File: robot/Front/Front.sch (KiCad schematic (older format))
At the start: 43 parts, among them J1 USB_B_Micro, Q1 BC849, Q2 BC849, SW2 SW_Push, U1 CH340C, U10 ESP32-WROOM-32, U2 CJVL53L0XV2, U3 LD1117S33CTR

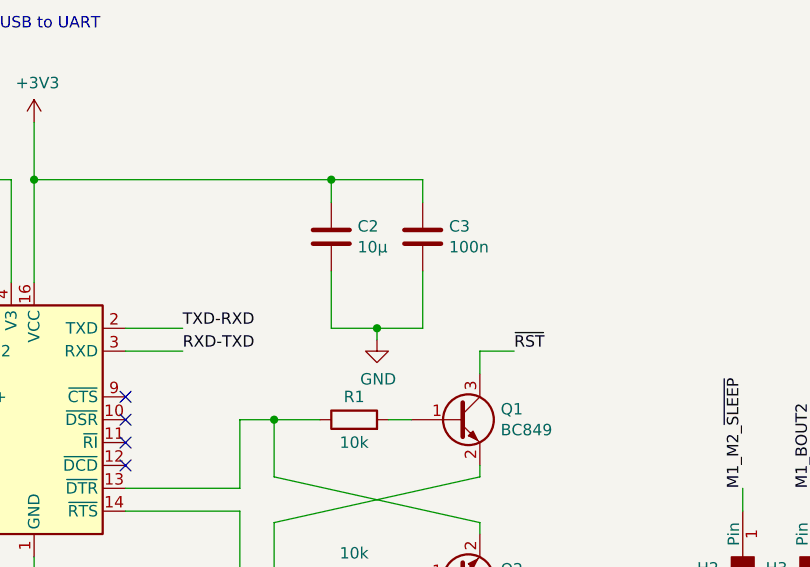
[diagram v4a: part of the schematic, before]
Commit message: Shrink design
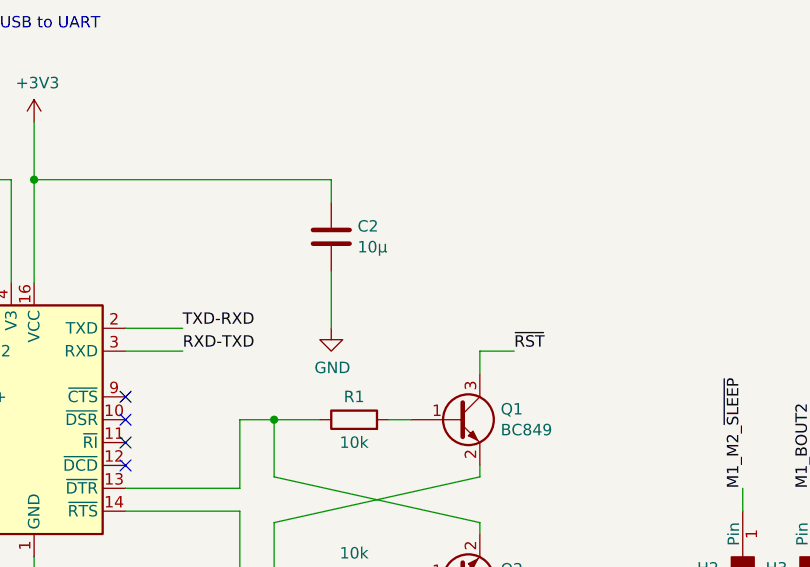
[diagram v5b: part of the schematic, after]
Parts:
- removed C3: 100n, Capacitors_SMD:C_1206, symbol Device:C
- C1, C2, C6: footprint Capacitors_SMD:C_1206 -> Capacitors_SMD:C_0805
- R1, R18, R2, R3, R4: footprint Resistors_SMD:R_1206 -> Resistors_SMD:R_0805
- U2: footprint Custom:CJVL53L0XV2_NoMountHoles -> Custom:GYVL53L0X_NoMountingHoles
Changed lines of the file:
@@
 F 0 "R18" H 8070 1196 50  0000 L CNN
 F 1 "10k" H 8070 1105 50  0000 L CNN
-F 2 "Resistors_SMD:R_1206" V 7930 1150 50  0001 C CNN
+F 2 "Resistors_SMD:R_0805" V 7930 1150 50  0001 C CNN
 F 3 "~" H 8000 1150 50  0001 C CNN
 	1    8000 1150
@@
 F 0 "C1" H 2365 1846 50  0000 L CNN
 F 1 "100n" H 2365 1755 50  0000 L CNN
-F 2 "Capacitors_SMD:C_1206" H 2288 1650 50  0001 C CNN
+F 2 "Capacitors_SMD:C_0805" H 2288 1650 50  0001 C CNN
 F 3 "~" H 2250 1800 50  0001 C CNN
 	1    2250 1800
@@
 $Comp
 L Device:C C?
-U 1 1 5D727709
-P 4450 1850
-AR Path="/5D17B31F/5D727709" Ref="C?"  Part="1"
-AR Path="/5D179377/5D727709" Ref="C?"  Part="1"
-AR Path="/5D727709" Ref="C3"  Part="1"
-F 0 "C3" H 4565 1896 50  0000 L CNN
-F 1 "100n" H 4565 1805 50  0000 L CNN
-F 2 "Capacitors_SMD:C_1206" H 4488 1700 50  0001 C CNN
-F 3 "~" H 4450 1850 50  0001 C CNN
-	1    4450 1850
-	1    0    0    -1
-$EndComp
-$Comp
-L Device:C C?
 U 1 1 5D72A7A5
 P 4050 1850
@@
 F 0 "C2" H 4165 1896 50  0000 L CNN
 F 1 "10µ" H 4165 1805 50  0000 L CNN
-F 2 "Capacitors_SMD:C_1206" H 4088 1700 50  0001 C CNN
+F 2 "Capacitors_SMD:C_0805" H 4088 1700 50  0001 C CNN
 F 3 "~" H 4050 1850 50  0001 C CNN
 	1    4050 1850
@@
 	4050 1700 4050 1600
 Wire Wire Line
-	4450 1700 4450 1600
-Wire Wire Line
-	4050 1600 4450 1600
-Wire Wire Line
 	2250 1950 2250 2050
 Wire Wire Line
@@
 L power:GND #PWR?
 U 1 1 5D72771A
-P 4250 2300
+P 4050 2250
 AR Path="/5D17B31F/5D72771A" Ref="#PWR?"  Part="1"
 AR Path="/5D179377/5D72771A" Ref="#PWR?"  Part="1"
 AR Path="/5D72771A" Ref="#PWR03"  Part="1"
-F 0 "#PWR03" H 4250 2050 50  0001 C CNN
-F 1 "GND" H 4255 2127 50  0000 C CNN
-F 2 "" H 4250 2300 50  0001 C CNN
-F 3 "" H 4250 2300 50  0001 C CNN
-	1    4250 2300
-	1    0    0    -1
-$EndComp
-Wire Wire Line
-	4250 2250 4450 2250
-Wire Wire Line
-	4450 2250 4450 2000
-Wire Wire Line
-	4250 2250 4250 2300
-Wire Wire Line
-	4050 2250 4250 2250
+F 0 "#PWR03" H 4050 2000 50  0001 C CNN
+F 1 "GND" H 4055 2077 50  0000 C CNN
+F 2 "" H 4050 2250 50  0001 C CNN
+F 3 "" H 4050 2250 50  0001 C CNN
+	1    4050 2250
+	1    0    0    -1
+$EndComp
 Wire Wire Line
 	4050 2000 4050 2250
-Connection ~ 4250 2250
 Wire Wire Line
 	2750 1600 4050 1600
@@
 Wire Wire Line
 	2750 1600 2750 2050
-Connection ~ 4050 1600
 NoConn ~ 3150 2550
 NoConn ~ 3150 2650
@@
 F 0 "R1" V 4250 2650 50  0000 C CNN
 F 1 "10k" V 4050 2650 50  0000 C CNN
-F 2 "Resistors_SMD:R_1206" V 4080 2650 50  0001 C CNN
+F 2 "Resistors_SMD:R_0805" V 4080 2650 50  0001 C CNN
 F 3 "~" H 4150 2650 50  0001 C CNN
 	1    4150 2650
@@
 F 0 "R2" V 4250 3350 50  0000 C CNN
 F 1 "10k" V 4034 3350 50  0000 C CNN
-F 2 "Resistors_SMD:R_1206" V 4080 3350 50  0001 C CNN
+F 2 "Resistors_SMD:R_0805" V 4080 3350 50  0001 C CNN
 F 3 "~" H 4150 3350 50  0001 C CNN
 	1    4150 3350
@@
 F 0 "R3" H 9630 5254 50  0000 R CNN
 F 1 "150" H 9630 5345 50  0000 R CNN
-F 2 "Resistors_SMD:R_1206" V 9630 5300 50  0001 C CNN
+F 2 "Resistors_SMD:R_0805" V 9630 5300 50  0001 C CNN
 F 3 "~" H 9700 5300 50  0001 C CNN
 	1    9700 5300
@@
 F 0 "R4" H 10630 5254 50  0000 R CNN
 F 1 "150" H 10630 5345 50  0000 R CNN
-F 2 "Resistors_SMD:R_1206" V 10630 5300 50  0001 C CNN
+F 2 "Resistors_SMD:R_0805" V 10630 5300 50  0001 C CNN
 F 3 "~" H 10700 5300 50  0001 C CNN
 	1    10700 5300
@@
 F 0 "U2" H 7800 5565 50  0000 C CNN
 F 1 "CJVL53L0XV2" H 7800 5474 50  0000 C CNN
-F 2 "Custom:CJVL53L0XV2_NoMountHoles" H 7800 5200 50  0001 C CNN
+F 2 "Custom:GYVL53L0X_NoMountingHoles" H 7800 5200 50  0001 C CNN
 F 3 "" H 7800 5200 50  0001 C CNN
 	1    7800 5000
@@
 F 0 "C6" H 2765 6096 50  0000 L CNN
 F 1 "10µ" H 2765 6005 50  0000 L CNN
-F 2 "Capacitors_SMD:C_1206" H 2688 5900 50  0001 C CNN
+F 2 "Capacitors_SMD:C_0805" H 2688 5900 50  0001 C CNN
 F 3 "~" H 2650 6050 50  0001 C CNN
 	1    2650 6050

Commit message: Finish Front redesign
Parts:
- removed C6: 10µ, Capacitors_SMD:C_0805, symbol Device:C
- removed U3: LD1117S33CTR, Package_TO_SOT_SMD:SOT-223, symbol dk_PMIC-Voltage-Regulators-Linear:LD1117S33CTR
- added U3: SPX3819M5-L-3-3, Package_TO_SOT_SMD:SOT-23-5, symbol Regulator_Linear:SPX3819M5-L-3-3
- C2: value 10µ -> 22µ
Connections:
- net +3V3: now also U3.5 (OUT)
- net BAT_MON: now also U10.6 (IO34); no longer U10.10 (IO25)
- net ED_IN1: now also U10.12 (IO27); no longer U10.6 (IO34)
- net ED_IN2: now also U10.27 (IO16); no longer U10.7 (IO35)
- net GND: now also U3.2 (GND)
- net OD_INTERRUPT: now also U10.31 (IO19); no longer U10.8 (IO32)
- net OD_SCL: now also U10.28 (IO17); no longer U10.14 (IO12)
- net OD_SDA: now also U10.29 (IO5); no longer U10.13 (IO14)
- net OD_SHUT: now also U10.30 (IO18); no longer U10.9 (IO33)
- net STATUS_LED_BLUE: now also U10.8 (IO32); no longer U10.30 (IO18)
- net STATUS_LED_GRN: now also U10.7 (IO35); no longer U10.31 (IO19)
- net VBUS: now also U3.1 (IN), U3.3 (EN)
- no-connect marks 16 -> 17
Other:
- moved on the sheet: R18, SW2
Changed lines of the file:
@@
 $EndDescr
-$Comp
-L RF_Module:ESP32-WROOM-32 U10
-U 1 1 5D72A796
-P 9250 2650
-F 0 "U10" H 9650 4000 50  0000 C CNN
-F 1 "ESP32-WROOM-32" H 8750 4000 50  0000 C CNN
-F 2 "RF_Module:ESP32-WROOM-32" H 9250 1150 50  0001 C CNN
-F 3 "https://www.espressif.com/sites/default/files/documentation/esp32-wroom-32_datasheet_en.pdf" H 8950 2700 50  0001 C CNN
-	1    9250 2650
-	1    0    0    -1
-$EndComp
 $Comp
 L power:+3V3 #PWR047
@@
 	9850 1750 10050 1750
 Wire Wire Line
-	7750 1450 8000 1450
+	7450 1450 7700 1450
 Wire Wire Line
 	9850 1450 10050 1450
@@
 L Switch:SW_Push SW2
 U 1 1 5D62C889
-P 8000 1800
-F 0 "SW2" V 8100 1650 50  0000 C CNN
-F 1 "SW_Push" V 7950 1550 50  0000 C CNN
-F 2 "Button_Switch_SMD:Panasonic_EVQPUJ_EVQPUA" H 8000 2000 50  0001 C CNN
-F 3 "~" H 8000 2000 50  0001 C CNN
-	1    8000 1800
+P 7700 1800
+F 0 "SW2" V 7800 1650 50  0000 C CNN
+F 1 "SW_Push" V 7650 1550 50  0000 C CNN
+F 2 "Button_Switch_SMD:Panasonic_EVQPUJ_EVQPUA" H 7700 2000 50  0001 C CNN
+F 3 "~" H 7700 2000 50  0001 C CNN
+	1    7700 1800
 	0    -1   -1   0
 $EndComp
@@
 L Device:R R18
 U 1 1 5D62DCB0
-P 8000 1150
-F 0 "R18" H 8070 1196 50  0000 L CNN
-F 1 "10k" H 8070 1105 50  0000 L CNN
-F 2 "Resistors_SMD:R_0805" V 7930 1150 50  0001 C CNN
-F 3 "~" H 8000 1150 50  0001 C CNN
-	1    8000 1150
+P 7700 1150
+F 0 "R18" H 7770 1196 50  0000 L CNN
+F 1 "10k" H 7770 1105 50  0000 L CNN
+F 2 "Resistors_SMD:R_0805" V 7630 1150 50  0001 C CNN
+F 3 "~" H 7700 1150 50  0001 C CNN
+	1    7700 1150
 	1    0    0    -1
 $EndComp
@@
 L power:+3V3 #PWR046
 U 1 1 5D62E308
-P 8000 900
-F 0 "#PWR046" H 8000 750 50  0001 C CNN
-F 1 "+3V3" H 8015 1073 50  0000 C CNN
-F 2 "" H 8000 900 50  0001 C CNN
-F 3 "" H 8000 900 50  0001 C CNN
-	1    8000 900
+P 7700 900
+F 0 "#PWR046" H 7700 750 50  0001 C CNN
+F 1 "+3V3" H 7715 1073 50  0000 C CNN
+F 2 "" H 7700 900 50  0001 C CNN
+F 3 "" H 7700 900 50  0001 C CNN
+	1    7700 900
 	1    0    0    -1
 $EndComp
@@
 L power:GND #PWR049
 U 1 1 5D62E7C3
-P 8000 2100
-F 0 "#PWR049" H 8000 1850 50  0001 C CNN
-F 1 "GND" H 8005 1927 50  0000 C CNN
-F 2 "" H 8000 2100 50  0001 C CNN
-F 3 "" H 8000 2100 50  0001 C CNN
-	1    8000 2100
-	1    0    0    -1
-$EndComp
-Wire Wire Line
-	8000 900  8000 1000
-Wire Wire Line
-	8000 1300 8000 1450
-Connection ~ 8000 1450
-Wire Wire Line
-	8000 1600 8000 1450
-Wire Wire Line
-	8000 2100 8000 2000
-Wire Wire Line
-	9850 2050 10050 2050
-Wire Wire Line
-	9850 2250 10050 2250
+P 7700 2100
+F 0 "#PWR049" H 7700 1850 50  0001 C CNN
+F 1 "GND" H 7705 1927 50  0000 C CNN
+F 2 "" H 7700 2100 50  0001 C CNN
+F 3 "" H 7700 2100 50  0001 C CNN
+	1    7700 2100
+	1    0    0    -1
+$EndComp
+Wire Wire Line
+	7700 900  7700 1000
+Wire Wire Line
+	7700 1300 7700 1450
+Connection ~ 7700 1450
+Wire Wire Line
+	7700 1600 7700 1450
+Wire Wire Line
+	7700 2100 7700 2000
 Wire Wire Line
 	9850 2950 10050 2950
@@
 Wire Wire Line
 	10050 2350 9850 2350
-Wire Wire Line
-	9850 3750 10050 3750
-Wire Wire Line
-	9850 3650 10050 3650
-Wire Wire Line
-	9850 3450 10050 3450
-Wire Wire Line
-	9850 3550 10050 3550
-Wire Wire Line
-	9850 3150 10050 3150
 Wire Wire Line
 	9850 2750 10050 2750
@@
 	9850 3050 10050 3050
 NoConn ~ 9850 1850
-NoConn ~ 9850 1950
-NoConn ~ 9850 2450
-NoConn ~ 9850 2550
 NoConn ~ 9850 3250
-NoConn ~ 9850 3350
-NoConn ~ 8650 1750
-NoConn ~ 8650 1650
 $Comp
 L Device:C C?
@@
 AR Path="/5D72A7A5" Ref="C2"  Part="1"
 F 0 "C2" H 4165 1896 50  0000 L CNN
-F 1 "10µ" H 4165 1805 50  0000 L CNN
+F 1 "22µ" H 4165 1805 50  0000 L CNN
 F 2 "Capacitors_SMD:C_0805" H 4088 1700 50  0001 C CNN
 F 3 "~" H 4050 1850 50  0001 C CNN
@@
 Wire Wire Line
 	3150 3050 3650 3050
-Text Notes 8300 850  0    50   ~ 0
+Text Notes 8000 850  0    50   ~ 0
 ESP32-WROOM
 Text Notes 2600 950  0    50   ~ 0
@@
 Text Label 10650 5000 2    50   ~ 0
 STATUS_LED_GRN
-Text Label 7750 1450 2    50   ~ 0
+Text Label 7450 1450 2    50   ~ 0
 ~RST
 Text Label 10050 1450 0    50   ~ 0
@@
 Text Label 10050 1550 0    50   ~ 0
 RXD-TXD
+Text Label 10050 3450 0    50   ~ 0
+STATUS_LED_BLUE
+Text Label 10050 3750 0    50   ~ 0
+STATUS_LED_GRN
+Text Label 10050 2550 0    50   ~ 0
+OD_SCL
+Text Label 10050 1950 0    50   ~ 0
+OD_SDA
+Text Label 10050 2750 0    50   ~ 0
+OD_INTERRUPT
 Text Label 10050 2650 0    50   ~ 0
-STATUS_LED_BLUE
-Text Label 10050 2750 0    50   ~ 0
-STATUS_LED_GRN
-Text Label 10050 2050 0    50   ~ 0
-OD_SCL
-Text Label 10050 2250 0    50   ~ 0
-OD_SDA
-Text Label 10050 3450 0    50   ~ 0
-OD_INTERRUPT
-Text Label 10050 3550 0    50   ~ 0
 OD_SHUT
 Text Label 8450 2650 2    50   ~ 0
@@
 Text Label 8450 3150 2    50   ~ 0
 M1_AOUT1
-Text Label 10050 3750 0    50   ~ 0
+Text Label 10050 2450 0    50   ~ 0
 ED_IN2
+Text Label 10050 3350 0    50   ~ 0
+ED_IN1
 Text Label 10050 3650 0    50   ~ 0
-ED_IN1
-Text Label 10050 3150 0    50   ~ 0
 BAT_MON
 Text Label 10050 3050 0    50   ~ 0
@@
 Text Label 10050 1650 0    50   ~ 0
 M1_M2_~SLEEP
-Wire Wire Line
-	1350 5850 1550 5850
 Connection ~ 1350 5850
 Wire Wire Line
@@
 $EndComp
 Wire Wire Line
-	2050 6350 2050 6250
-Wire Wire Line
-	2000 6350 2050 6350
-Wire Wire Line
-	1950 6250 1950 6350
-Wire Wire Line
-	2000 6350 2000 6400
-Connection ~ 2000 6350
-Wire Wire Line
-	1950 6350 2000 6350
-$Comp
-L power:GND #PWR022
-U 1 1 5D7374A2
-P 2000 6400
-F 0 "#PWR022" H 2000 6150 50  0001 C CNN
-F 1 "GND" H 2005 6227 50  0000 C CNN
-F 2 "" H 2000 6400 50  0001 C CNN
-F 3 "" H 2000 6400 50  0001 C CNN
-	1    2000 6400
-	1    0    0    -1
-$EndComp
-Wire Wire Line
 	2650 5500 2650 5850
-Wire Wire Line
-	2650 6200 2650 6250
-Connection ~ 2650 5850
-Wire Wire Line
-	2650 5850 2650 5900
-$Comp
-L Device:C C6
-U 1 1 5D7374B6
-P 2650 6050
-F 0 "C6" H 2765 6096 50  0000 L CNN
-F 1 "10µ" H 2765 6005 50  0000 L CNN
-F 2 "Capacitors_SMD:C_0805" H 2688 5900 50  0001 C CNN
-F 3 "~" H 2650 6050 50  0001 C CNN
-	1    2650 6050
-	1    0    0    -1
-$EndComp
-$Comp
-L power:GND #PWR021
-U 1 1 5D7374BC
-P 2650 6250
-F 0 "#PWR021" H 2650 6000 50  0001 C CNN
-F 1 "GND" H 2655 6077 50  0000 C CNN
-F 2 "" H 2650 6250 50  0001 C CNN
-F 3 "" H 2650 6250 50  0001 C CNN
-	1    2650 6250
-	1    0    0    -1
-$EndComp
 $Comp
 L power:+3V3 #PWR015
@@
 $EndComp
 $Comp
-L dk_PMIC-Voltage-Regulators-Linear:LD1117S33CTR U3
-U 1 1 5D7374D1
-P 1950 5850
-F 0 "U3" H 2000 6137 60  0000 C CNN
-F 1 "LD1117S33CTR" H 2000 6031 60  0000 C CNN
-F 2 "Package_TO_SOT_SMD:SOT-223" H 2150 6050 60  0001 L CNN
-F 3 "http://www.st.com/content/ccc/resource/technical/document/datasheet/99/3b/7d/91/91/51/4b/be/CD00000544.pdf/files/CD00000544.pdf/jcr:content/translations/en.CD00000544.pdf" H 2150 6150 60  0001 L CNN
-F 4 "497-1241-1-ND" H 2150 6250 60  0001 L CNN "Digi-Key_PN"
-F 5 "LD1117S33CTR" H 2150 6350 60  0001 L CNN "MPN"
-F 6 "Integrated Circuits (ICs)" H 2150 6450 60  0001 L CNN "Category"
-F 7 "PMIC - Voltage Regulators - Linear" H 2150 6550 60  0001 L CNN "Family"
-F 8 "http://www.st.com/content/ccc/resource/technical/document/datasheet/99/3b/7d/91/91/51/4b/be/CD00000544.pdf/files/CD00000544.pdf/jcr:content/translations/en.CD00000544.pdf" H 2150 6650 60  0001 L CNN "DK_Datasheet_Link"
-F 9 "/product-detail/en/stmicroelectronics/LD1117S33CTR/497-1241-1-ND/586241" H 2150 6750 60  0001 L CNN "DK_Detail_Page"
-F 10 "IC REG LINEAR 3.3V 800MA SOT223" H 2150 6850 60  0001 L CNN "Description"
-F 11 "STMicroelectronics" H 2150 6950 60  0001 L CNN "Manufacturer"
-F 12 "Active" H 2150 7050 60  0001 L CNN "Status"
-	1    1950 5850
-	1    0    0    -1
-$EndComp
-$Comp
 L Connector:USB_B_Micro J1
 U 1 1 5D7374D7
@@
 Text Notes 4600 4800 0    50   ~ 0
 PADS TOP
-Wire Wire Line
-	2450 5850 2650 5850
 $Comp
 L Custom:MountingPad H1
@@
 NoConn ~ 2350 2850
 NoConn ~ 2350 3050
-Wire Wire Line
-	8000 1450 8650 1450
 $Comp
 L Custom:MountingPad H24
@@
 Text Label 1500 2200 0    50   ~ 0
 D-
+$Comp
+L power:GND #PWR022
+U 1 1 5D7374A2
+P 1950 6350
+F 0 "#PWR022" H 1950 6100 50  0001 C CNN
+F 1 "GND" H 1955 6177 50  0000 C CNN
+F 2 "" H 1950 6350 50  0001 C CNN
+F 3 "" H 1950 6350 50  0001 C CNN
+	1    1950 6350
+	1    0    0    -1
+$EndComp
+Wire Wire Line
+	1950 6250 1950 6350
+Wire Wire Line
+	1350 5850 1550 5850
+Wire Wire Line
+	1550 5850 1550 5950
+Wire Wire Line
+	1550 5950 1650 5950
+Connection ~ 1550 5850
+Wire Wire Line
+	1550 5850 1650 5850
+Wire Wire Line
+	2250 5850 2650 5850
+NoConn ~ 2250 5950
+$Comp
+L Regulator_Linear:SPX3819M5-L-3-3 U3
+U 1 1 5D92E82C
+P 1950 5950
+F 0 "U3" H 1950 6292 50  0000 C CNN
+F 1 "SPX3819M5-L-3-3" H 1950 6201 50  0000 C CNN
+F 2 "Package_TO_SOT_SMD:SOT-23-5" H 1950 6275 50  0001 C CNN
+F 3 "https://www.exar.com/content/document.ashx?id=22106&languageid=1033&type=Datasheet&partnumber=SPX3819&filename=SPX3819.pdf&part=SPX3819" H 1950 5950 50  0001 C CNN
+	1    1950 5950
+	1    0    0    -1
+$EndComp
+Wire Wire Line
+	9850 3350 10050 3350
+Wire Wire Line
+	9850 2450 10050 2450
+$Comp
+L RF_Module:ESP32-WROOM-32 U10
+U 1 1 5D72A796
+P 9250 2650
+F 0 "U10" H 9650 4000 50  0000 C CNN
+F 1 "ESP32-WROOM-32" H 8750 4000 50  0000 C CNN
+F 2 "RF_Module:ESP32-WROOM-32" H 9250 1150 50  0001 C CNN
+F 3 "https://www.espressif.com/sites/default/files/documentation/esp32-wroom-32_datasheet_en.pdf" H 8950 2700 50  0001 C CNN
+	1    9250 2650
+	1    0    0    -1
+$EndComp
+Wire Wire Line
+	7700 1450 8650 1450
+Wire Wire Line
+	9850 1950 10050 1950
+Wire Wire Line
+	10050 2550 9850 2550
+NoConn ~ 9850 2050
+NoConn ~ 9850 2250
+NoConn ~ 9850 3550
+Wire Wire Line
+	9850 3750 10050 3750
+Wire Wire Line
+	10050 3450 9850 3450
+NoConn ~ 8650 1650
+NoConn ~ 8650 1750
+Wire Wire Line
+	10050 3650 9850 3650
+NoConn ~ 9850 3150
 $EndSCHEMATC

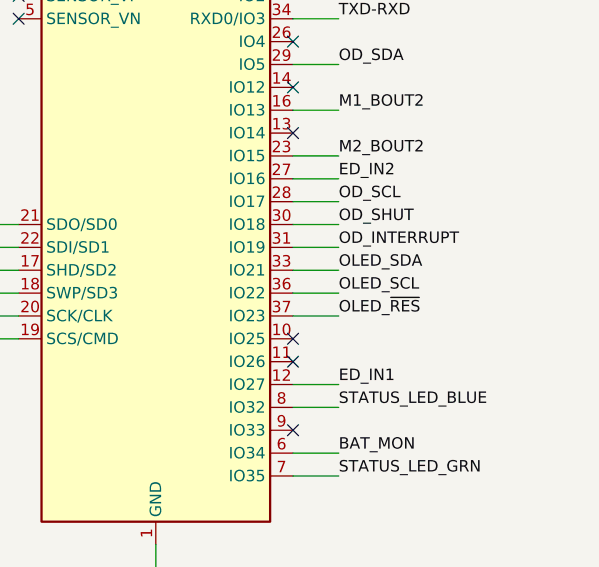
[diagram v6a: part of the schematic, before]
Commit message: Finish Top, remap OLED pins
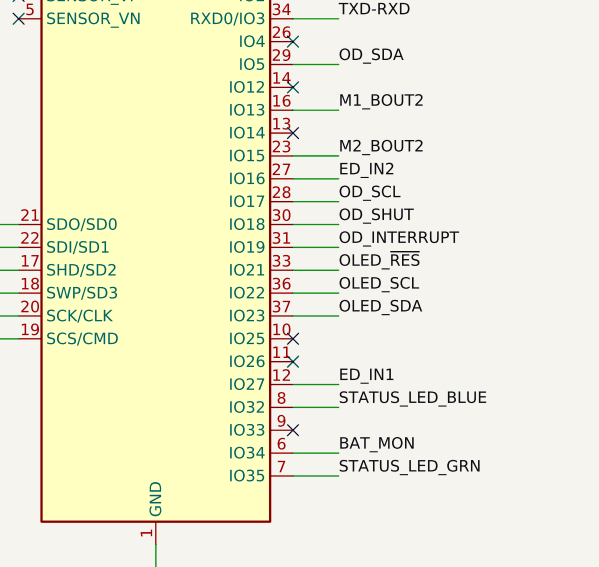
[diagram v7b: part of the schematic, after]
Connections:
- net OLED_SDA: now also U10.37 (IO23); no longer U10.33 (IO21)
- net OLED_~RES: now also U10.33 (IO21); no longer U10.37 (IO23)
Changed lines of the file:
@@
 Text Label 10050 3650 0    50   ~ 0
 BAT_MON
-Text Label 10050 3050 0    50   ~ 0
+Text Label 10050 2850 0    50   ~ 0
 OLED_~RES
 Text Label 10050 2950 0    50   ~ 0
 OLED_SCL
-Text Label 10050 2850 0    50   ~ 0
+Text Label 10050 3050 0    50   ~ 0
 OLED_SDA
 Text Label 10050 2350 0    50   ~ 0
